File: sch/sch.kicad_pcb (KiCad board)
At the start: 2 copper layers, 17.8 x 43.2 mm, 6 parts, among them P1 Digital, P2 Analog, P3 CONN_1, P4 CONN_1, P5 CONN_1, P6 CONN_1

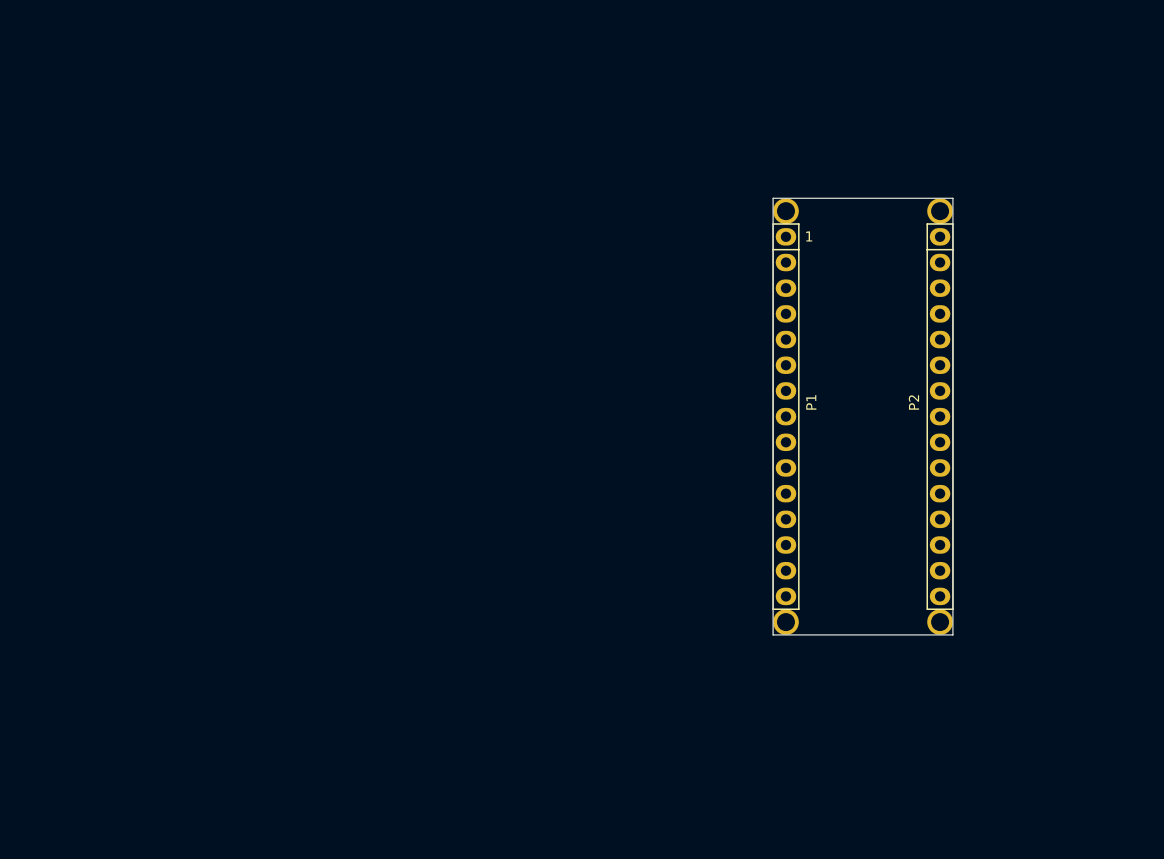
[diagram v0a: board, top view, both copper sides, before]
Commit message: Schematic ready for layout, started layout work
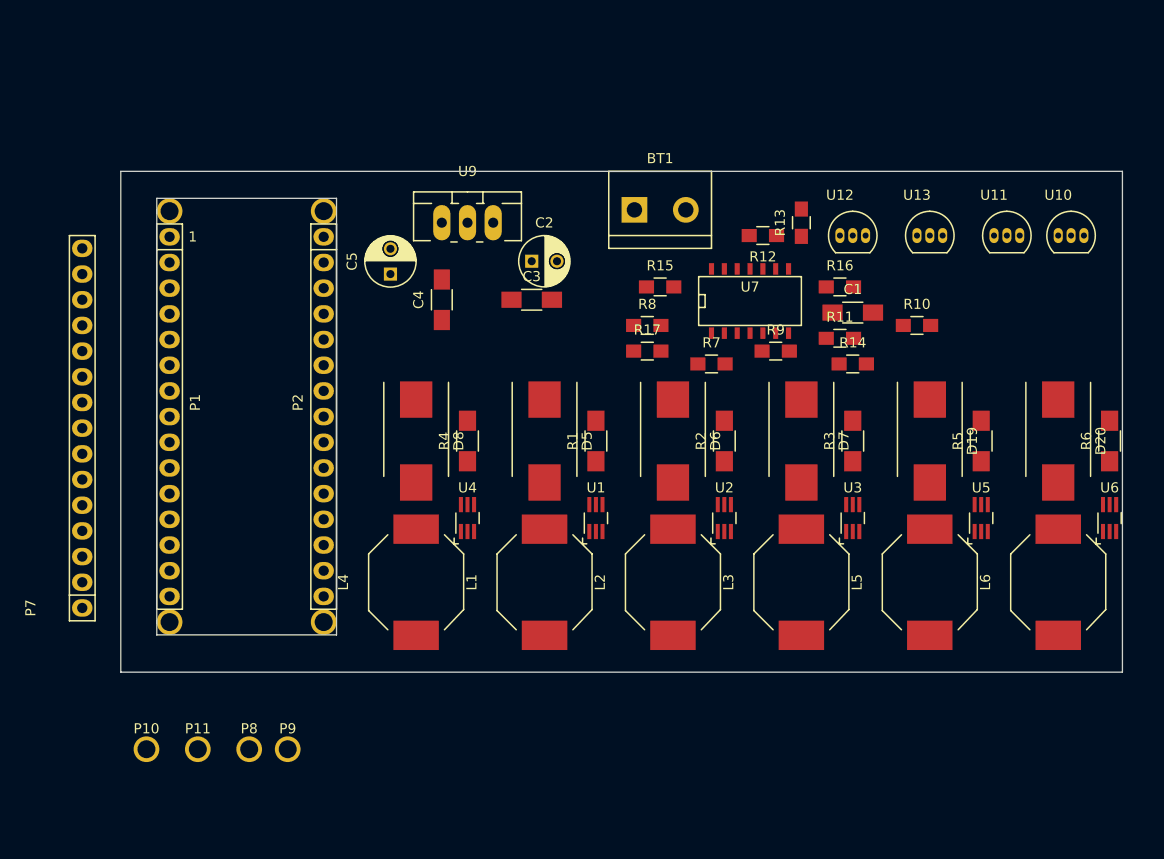
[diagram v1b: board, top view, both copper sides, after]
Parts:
- added BT1: Battery, Connect:bornier2, F.Cu at (127.0, 68.6)
- added C1: C, Capacitors_SMD:C_1206_HandSoldering, F.Cu at (146.1, 78.7)
- added C2: CP, Capacitors_ThroughHole:C_Radial_D5_L6_P2.5, F.Cu at (114.3, 73.7)
- added C3: C, Capacitors_SMD:C_1206_HandSoldering, F.Cu at (114.3, 77.5)
- added C4: C, Capacitors_SMD:C_1206_HandSoldering, F.Cu at (105.4, 77.5)
- added C5: CP, Capacitors_ThroughHole:C_Radial_D5_L6_P2.5, F.Cu at (100.3, 74.9)
- added D19: D_Schottky, Diodes_SMD:DO-214AB_Handsoldering, F.Cu at (153.7, 91.4)
- added D20: D_Schottky, Diodes_SMD:DO-214AB_Handsoldering, F.Cu at (166.4, 91.4)
- added D5: D_Schottky, Diodes_SMD:DO-214AB_Handsoldering, F.Cu at (115.6, 91.4)
- added D6: D_Schottky, Diodes_SMD:DO-214AB_Handsoldering, F.Cu at (128.3, 91.4)
- added D7: D_Schottky, Diodes_SMD:DO-214AB_Handsoldering, F.Cu at (141.0, 91.4)
- added D8: D_Schottky, Diodes_SMD:DO-214AB_Handsoldering, F.Cu at (102.9, 91.4)
- added L1: INDUCTOR, Inductors_NEOSID:Neosid_Inductor_Ms95, F.Cu at (115.6, 105.4)
- added L2: INDUCTOR, Inductors_NEOSID:Neosid_Inductor_Ms95, F.Cu at (128.3, 105.4)
- added L3: INDUCTOR, Inductors_NEOSID:Neosid_Inductor_Ms95, F.Cu at (141.0, 105.4)
- added L4: INDUCTOR, Inductors_NEOSID:Neosid_Inductor_Ms95, F.Cu at (102.9, 105.4)
- added L5: INDUCTOR, Inductors_NEOSID:Neosid_Inductor_Ms95, F.Cu at (153.7, 105.4)
- added L6: INDUCTOR, Inductors_NEOSID:Neosid_Inductor_Ms95, F.Cu at (166.4, 105.4)
- added P10: CONN_1, Socket_Arduino_Nano:1pin_Nano, F.Cu at (76.2, 121.9)
- added P11: CONN_1, Socket_Arduino_Nano:1pin_Nano, F.Cu at (81.3, 121.9)
- added P7: Analog, Socket_Arduino_Nano:Socket_Strip_Arduino_1x15, F.Cu at (69.8, 108.0)
- added P8: CONN_1, Socket_Arduino_Nano:1pin_Nano, F.Cu at (86.4, 121.9)
- added P9: CONN_1, Socket_Arduino_Nano:1pin_Nano, F.Cu at (90.2, 121.9)
- added R1: 0.13, Resistors_SMD:R_1206_HandSoldering, F.Cu at (120.7, 91.4)
- added R10: R, Resistors_SMD:R_0805_HandSoldering, F.Cu at (152.4, 80.0)
- added R11: R, Resistors_SMD:R_0805_HandSoldering, F.Cu at (144.8, 81.3)
- added R12: R, Resistors_SMD:R_0805_HandSoldering, F.Cu at (137.2, 71.1)
- added R13: R, Resistors_SMD:R_0805_HandSoldering, F.Cu at (141.0, 69.8)
- added R14: R, Resistors_SMD:R_0805_HandSoldering, F.Cu at (146.1, 83.8)
- added R15: R, Resistors_SMD:R_0805_HandSoldering, F.Cu at (127.0, 76.2)
- added R16: R, Resistors_SMD:R_0805_HandSoldering, F.Cu at (144.8, 76.2)
- added R17: R, Resistors_SMD:R_0805_HandSoldering, F.Cu at (125.7, 82.5)
- added R2: 0.13, Resistors_SMD:R_1206_HandSoldering, F.Cu at (133.3, 91.4)
- added R3: 0.13, Resistors_SMD:R_1206_HandSoldering, F.Cu at (146.1, 91.4)
- added R4: 0.13, Resistors_SMD:R_1206_HandSoldering, F.Cu at (108.0, 91.4)
- added R5: 0.13, Resistors_SMD:R_1206_HandSoldering, F.Cu at (158.8, 91.4)
- added R6: 0.13, Resistors_SMD:R_1206_HandSoldering, F.Cu at (171.4, 91.4)
- added R7: R, Resistors_SMD:R_0805_HandSoldering, F.Cu at (132.1, 83.8)
- added R8: R, Resistors_SMD:R_0805_HandSoldering, F.Cu at (125.7, 80.0)
- added R9: R, Resistors_SMD:R_0805_HandSoldering, F.Cu at (138.4, 82.5)
- added U1: PT4115, TO_SOT_Packages_SMD:SC-70-6_Handsoldering, F.Cu at (120.7, 99.1)
- added U10: DS18B20, TO_SOT_Packages_THT:TO-92_Inline_Narrow_Oval, F.Cu at (166.4, 71.1)
- added U11: DS18B20, TO_SOT_Packages_THT:TO-92_Inline_Narrow_Oval, F.Cu at (160.0, 71.1)
- added U12: DS18B20, TO_SOT_Packages_THT:TO-92_Inline_Narrow_Oval, F.Cu at (144.8, 71.1)
- added U13: DS18B20, TO_SOT_Packages_THT:TO-92_Inline_Narrow_Oval, F.Cu at (152.4, 71.1)
- added U2: PT4115, TO_SOT_Packages_SMD:SC-70-6_Handsoldering, F.Cu at (133.3, 99.1)
- added U3: PT4115, TO_SOT_Packages_SMD:SC-70-6_Handsoldering, F.Cu at (146.1, 99.1)
- added U4: PT4115, TO_SOT_Packages_SMD:SC-70-6_Handsoldering, F.Cu at (108.0, 99.1)
- added U5: PT4115, TO_SOT_Packages_SMD:SC-70-6_Handsoldering, F.Cu at (158.8, 99.1)
- added U6: PT4115, TO_SOT_Packages_SMD:SC-70-6_Handsoldering, F.Cu at (171.4, 99.1)
- added U7: LM324, SMD_Packages:SOIC-14_N, F.Cu at (135.9, 77.5)
- added U9: 7805, TO_SOT_Packages_THT:TO-220_Neutral123_Vertical_LargePads, F.Cu at (108.0, 69.8)
- P1: value Digital -> CONN_01X02
- P2: value Analog -> CONN_02X05
- P3, P4: value CONN_1 -> CONN_01X06
- P5: value CONN_1 -> BNC
- P6: value CONN_1 -> Digital
- moved P2 61.0 mm to (93.7, 71.2)
- moved P5 61.0 mm to (93.7, 109.3)
- moved P6 61.0 mm to (93.7, 68.7)
- moved P1 61.0 mm to (78.5, 71.2)
- moved P3 61.0 mm to (78.5, 68.7)
- moved P4 61.0 mm to (78.5, 109.3)
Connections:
- net Net-(P3-Pad1) renamed /MEAS_PROBE
- P1 pad 1: /1(Tx) -> /A3
- P1 pad 10: /7 -> (no net)
- P1 pad 11: /8 -> (no net)
- P1 pad 12: /9(**) -> (no net)
- P1 pad 13: /10(**/SS) -> (no net)
- P1 pad 14: /11(**/MISO) -> (no net)
- P1 pad 15: /12(MOSI) -> (no net)
- P1 pad 2: /0(Rx) -> GND
- P1 pad 3: /Reset -> (no net)
- P1 pad 4: GND -> (no net)
- P1 pad 5: /2 -> (no net)
- P1 pad 6: /3(**) -> (no net)
- P1 pad 7: /4 -> (no net)
- P1 pad 8: /5(**) -> (no net)
- P1 pad 9: /6(**) -> (no net)
- P2 pad 1: /Vin -> /3(**)
- P2 pad 10: /A2 -> GND
- P2 pad 11: /A1 -> (no net)
- P2 pad 12: /A0 -> (no net)
- P2 pad 13: /AREF -> (no net)
- P2 pad 14: +3.3V -> (no net)
- P2 pad 15: /13(SCK) -> (no net)
- P2 pad 2: GND -> /5(**)
- P2 pad 3: /Reset -> /6(**)
- P2 pad 4: +5V -> /9(**)
- P2 pad 5: /A7 -> /10(**/SS)
- P2 pad 6: /A6 -> /11(**/MISO)
- P2 pad 7: /A5 -> /2
- P2 pad 8: /A4 -> /4
- P2 pad 9: /A3 -> GND
- P4 pad 1: Net-(P4-Pad1) -> /12(MOSI)
- P5 pad 1: Net-(P5-Pad1) -> /PH
- P6 pad 1: Net-(P6-Pad1) -> /1(Tx)
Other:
- board size 17.8 x 43.2 mm -> 99.1 x 49.5 mm

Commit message: Started placement
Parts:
- added D13: LED, led:POWER_LED, B.Cu at (167.6, 88.9)
- added D14: LED, led:POWER_LED, B.Cu at (104.1, 90.2)
- added D15: LED, led:POWER_LED, B.Cu at (154.9, 88.9)
- added D16: LED, led:POWER_LED, B.Cu at (142.2, 88.9)
- added D21: LED, led:POWER_LED, B.Cu at (129.5, 94.0)
- added D23: LED, led:POWER_LED, B.Cu at (129.5, 83.8)
- added D24: LED, led:POWER_LED, B.Cu at (116.8, 91.4)
- D19, D20, D5, D6, D7, D8, R2, R6, U2, U5, U6: moved to B.Cu
- P1: footprint Socket_Arduino_Nano:Socket_Strip_Arduino_1x15 -> Connect:PINHEAD1-2
- P2: footprint Socket_Arduino_Nano:Socket_Strip_Arduino_1x15 -> Connect:IDC_Header_Straight_10pins; moved to B.Cu
- P3, P4: footprint Socket_Arduino_Nano:1pin_Nano -> Connect:PINHEAD1-6
- P5: footprint Socket_Arduino_Nano:1pin_Nano -> Connect:bnc-ci
- P6: footprint Socket_Arduino_Nano:1pin_Nano -> Socket_Arduino_Nano:Socket_Strip_Arduino_1x15
- U9: value 7805 -> LM7805CT; footprint TO_SOT_Packages_THT:TO-220_Neutral123_Vertical_LargePads -> Power_Integrations:TO-220
- moved P5 82.1 mm to (166.4, 71.1)
- moved P8 75.3 mm to (161.3, 129.5)
- moved P3 69.0 mm to (146.1, 54.6)
- moved D20 57.1 mm to (111.8, 108.0), turned to 90 degrees
- moved R6 56.7 mm to (116.8, 106.7), turned to 270 degrees
- moved U6 56.1 mm to (116.8, 111.8), turned to 90 degrees
- moved L1 52.1 mm to (167.6, 106.7)
- moved D5 49.8 mm to (162.6, 108.0), turned to 90 degrees
- moved L6 49.5 mm to (116.8, 106.7)
- moved C3 49.0 mm to (153.7, 106.7), turned to 90 degrees
- moved U1 48.9 mm to (168.9, 106.7)
- moved BT1 48.3 mm to (78.7, 68.6)
- moved R1 48.2 mm to (166.4, 106.7)
- moved P4 42.8 mm to (91.4, 68.6), turned to 180 degrees
- moved P6 41.8 mm to (95.2, 110.5), turned to 90 degrees
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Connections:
- U9 pad 1: (no net) -> +BATT
- U9 pad 2: (no net) -> GND
- U9 pad 3: (no net) -> +5V
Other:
- outline, holes or cut-outs redrawn
- board text removed: "1"

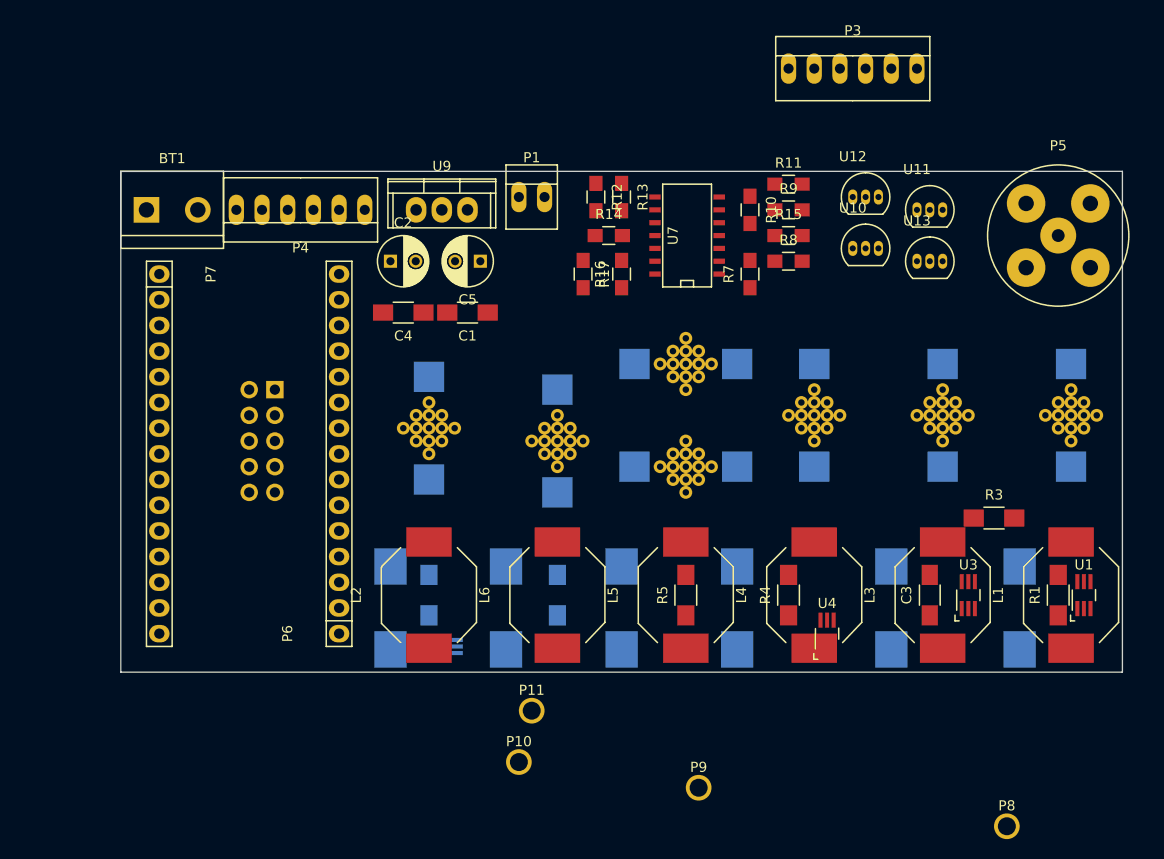
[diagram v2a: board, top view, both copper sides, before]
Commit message: Added some footprint libraries and started layout
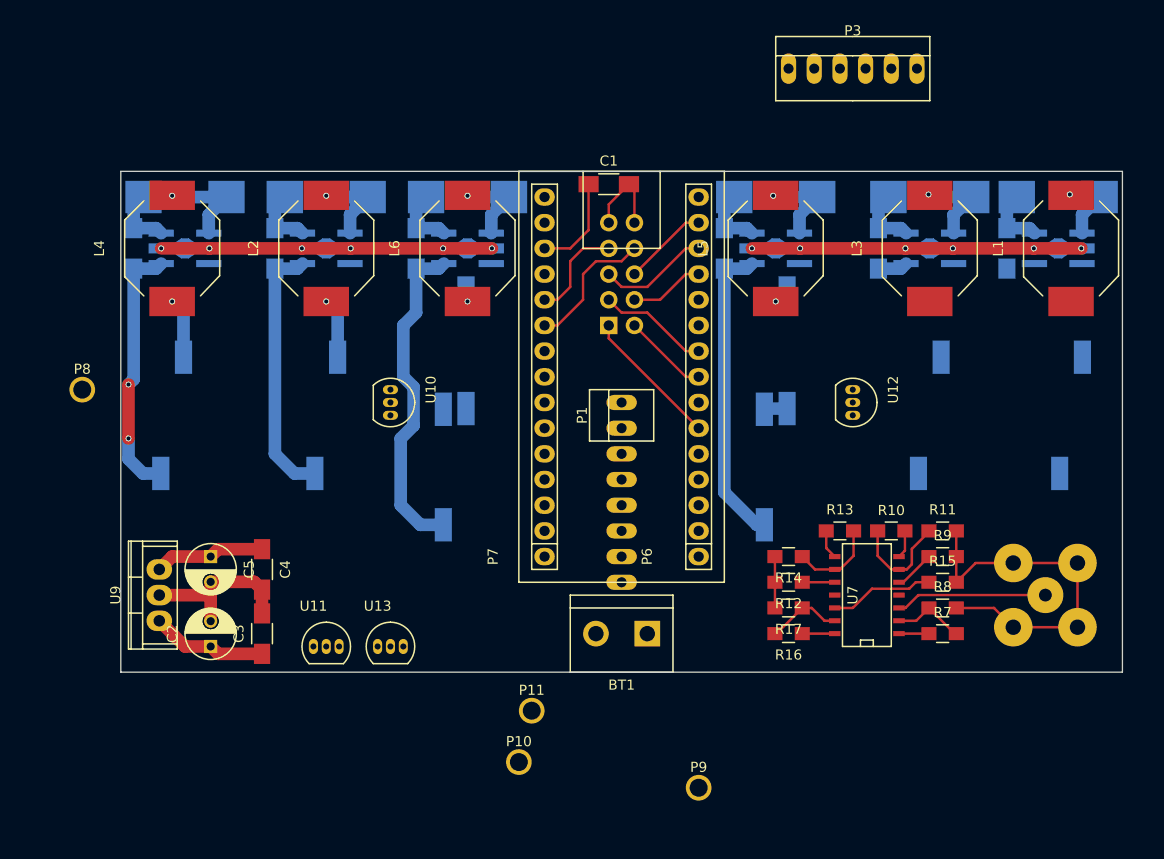
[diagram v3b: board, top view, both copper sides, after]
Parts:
- removed D13, D14, D15, D16, D21, D23, D24: LED, led:POWER_LED
- added D1: LED_PWR, sch:lumiled-2-LAMBERTIAN, B.Cu at (167.6, 88.9)
- added D10: LED_PWR, sch:lumiled-2-LAMBERTIAN, B.Cu at (138.4, 82.5)
- added D11: LED_PWR, sch:lumiled-2-LAMBERTIAN, B.Cu at (138.4, 94.0)
- added D12: LED_PWR, sch:lumiled-2-LAMBERTIAN, B.Cu at (106.7, 94.0)
- added D2: LED_PWR, sch:lumiled-2-LAMBERTIAN, B.Cu at (94.0, 88.9)
- added D3: LED_PWR, sch:lumiled-2-LAMBERTIAN, B.Cu at (153.7, 88.9)
- added D4: LED_PWR, sch:lumiled-2-LAMBERTIAN, B.Cu at (78.7, 88.9)
- added D9: LED_PWR, sch:lumiled-2-LAMBERTIAN, B.Cu at (106.7, 82.5)
- P4, P5, R1, R3, R4, R5: moved to B.Cu
- U1, U3, U4: footprint TO_SOT_Packages_SMD:SC-70-6_Handsoldering -> TO_SOT_Packages_SMD:SOT89-5_Housing_Handsoldering; moved to B.Cu
- U2, U5, U6: footprint TO_SOT_Packages_SMD:SC-70-6_Handsoldering -> TO_SOT_Packages_SMD:SOT89-5_Housing_Handsoldering
- moved P8 101.1 mm to (69.8, 86.4)
- moved U4 74.1 mm to (80.0, 72.4), turned to 270 degrees
- moved U11 73.7 mm to (92.7, 111.8)
- moved R4 73.3 mm to (74.9, 72.4)
- moved L4 72.2 mm to (78.7, 72.4)
- moved D8 68.1 mm to (80.0, 67.3), turned to 0 degrees
- moved C3 66.1 mm to (87.6, 110.5)
- moved U13 65.5 mm to (99.1, 111.8)
- moved BT1 61.1 mm to (123.2, 110.5), turned to 180 degrees
- moved U10 47.8 mm to (100.3, 86.4), turned to 270 degrees
- moved U9 47.2 mm to (77.5, 106.7), turned to 90 degrees
- moved P7 47.2 mm to (115.6, 102.9), turned to 90 degrees
- moved P4 44.0 mm to (123.2, 99.1), turned to 90 degrees
- moved D19 43.4 mm to (138.4, 67.3), turned to 0 degrees
- moved R12 42.6 mm to (139.7, 105.4), turned to 180 degrees
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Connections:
- U1 pad 5: GND -> +BATT
- U2 pad 5: GND -> +BATT
- U3 pad 5: GND -> +BATT
- U4 pad 5: GND -> +BATT
- U5 pad 5: GND -> +BATT
- U6 pad 5: GND -> +BATT
- U7 pad 4: +BATT -> +5V
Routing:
- net GND: track 0.00 -> 133.4 mm, vias 0 -> 12
- net +BATT: track 0.00 -> 50.0 mm
- net Net-(D12-PadANOD): track 0.00 -> 32.8 mm
- net Net-(D11-PadANOD): track 0.00 -> 30.4 mm
- net Net-(D2-PadANOD): track 0.00 -> 26.0 mm
- net Net-(D4-PadANOD): track 0.00 -> 25.8 mm, vias 0 -> 2
- net /PH: track 0.00 -> 15.0 mm
- net /3(**): track 0.00 -> 13.8 mm
- net /4: track 0.00 -> 13.5 mm
- net Net-(R10-Pad2): track 0.00 -> 11.6 mm
- net /6(**): track 0.00 -> 11.0 mm
- net /10(**/SS): track 0.00 -> 11.0 mm
- net +5V: track 0.00 -> 11.0 mm
- net /O_CAL1: track 0.00 -> 10.4 mm
- net /2: track 0.00 -> 9.94 mm
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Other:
- net class Medium added: clearance 0.2, trace_width 1.25, via_dia 0.6, via_drill 0.4

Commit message: continued routing
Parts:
- moved BT1 22.1 mm to (101.1, 110.0), turned to 0 degrees
- moved U13 18.3 mm to (117.3, 111.5)
- moved U11 17.3 mm to (110.0, 112.0)
- moved P4 12.8 mm to (129.0, 110.5), turned to 0 degrees
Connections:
- U1 pad 3: /3(**) -> /6(**)
- U2 pad 3: /5(**) -> /9(**)
- U3 pad 3: /6(**) -> /3(**)
- U4 pad 3: /9(**) -> /5(**)
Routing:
- net GND: track 133.4 -> 193.5 mm, vias 12 -> 14
- net /12(MOSI): track 2.78 -> 56.6 mm, vias 0 -> 1
- net /A0: track 3.22 -> 49.7 mm
- net /13(SCK): track 2.89 -> 49.4 mm, vias 0 -> 1
- net /5(**): track 8.45 -> 53.2 mm, vias 0 -> 2
- net /6(**): track 11.0 -> 54.6 mm, vias 0 -> 3
- net /3(**): track 13.8 -> 53.8 mm, vias 0 -> 4
- net +5V: track 11.0 -> 45.9 mm
- net /9(**): track 7.40 -> 37.2 mm, vias 0 -> 2
- net Net-(D1-PadANOD): track 0.00 -> 25.4 mm
- net /O_MEAS: track 4.02 -> 28.9 mm, vias 0 -> 1
- net Net-(D3-PadANOD): track 2.93 -> 24.8 mm
- net /2: track 9.94 -> 29.4 mm
- net /4: track 13.5 -> 32.2 mm
- net /11(**/MISO): track 8.45 -> 23.2 mm
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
